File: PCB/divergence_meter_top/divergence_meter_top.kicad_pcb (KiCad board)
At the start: 2 copper layers, 120.6 x 38.1 mm, 11 parts

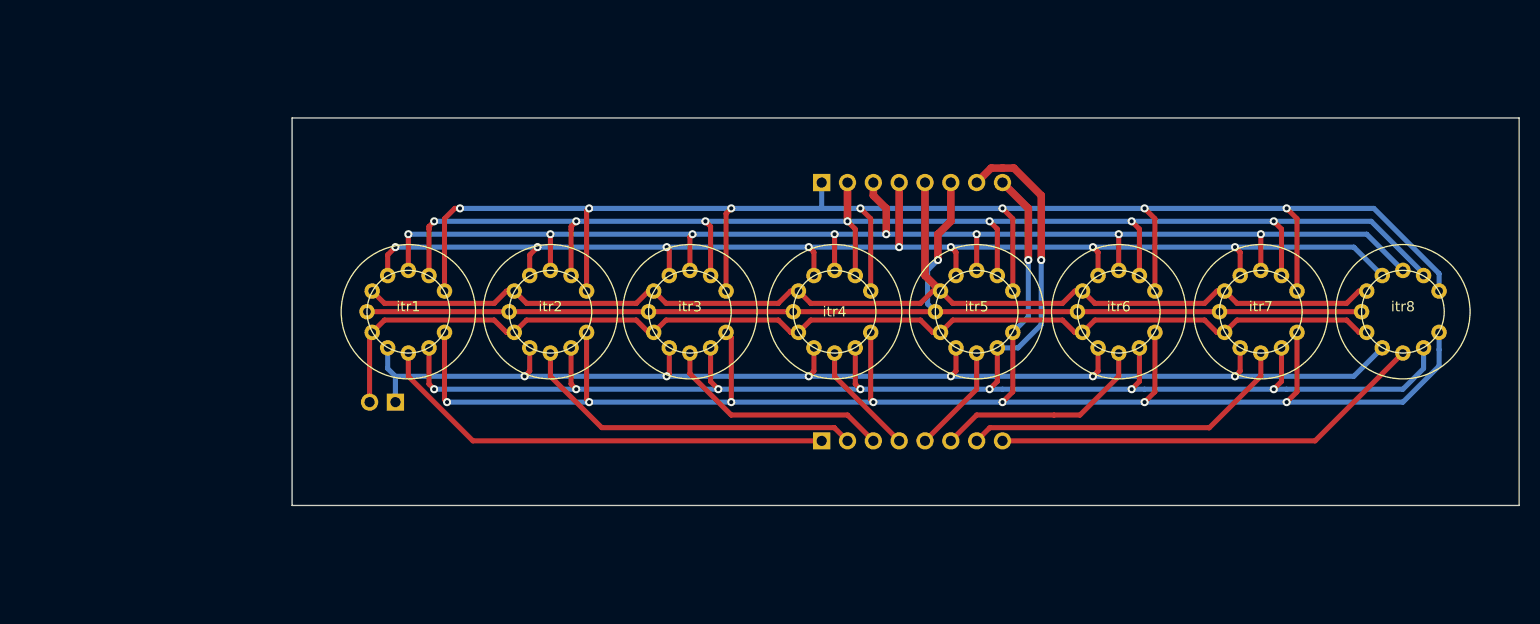
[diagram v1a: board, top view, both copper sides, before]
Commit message: logic pcb almost finished, remaking top
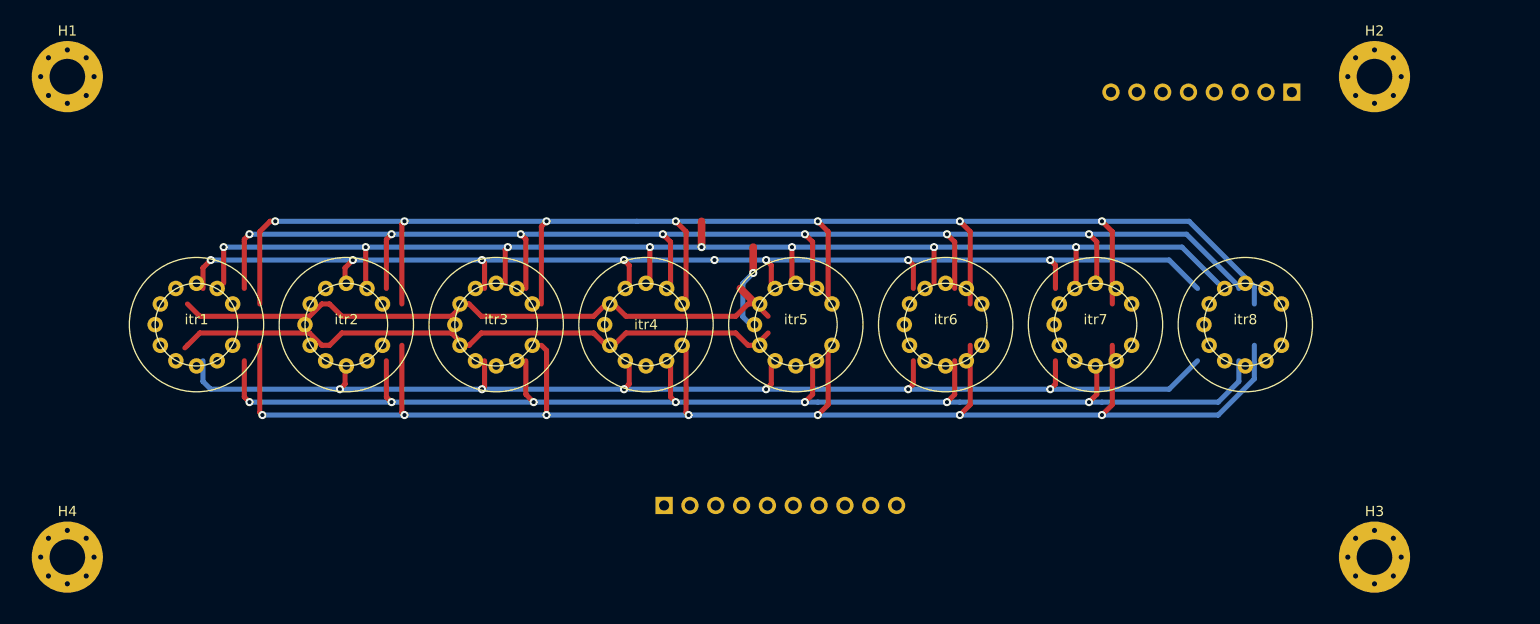
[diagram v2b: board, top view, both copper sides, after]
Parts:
- removed JG1: Conn_01x08, Connector_PinHeader_2.54mm:PinHeader_1x08_P2.54mm_Vertical
- removed JP1: 1V, Connector_PinHeader_2.54mm:PinHeader_1x02_P2.54mm_Vertical
- added H1: MountingHole_Pad, MountingHole:MountingHole_3.5mm_Pad_Via, F.Cu at (68.1, 84.8)
- added H2: MountingHole_Pad, MountingHole:MountingHole_3.5mm_Pad_Via, F.Cu at (196.6, 84.8)
- added H3: MountingHole_Pad, MountingHole:MountingHole_3.5mm_Pad_Via, F.Cu at (196.6, 132.1)
- added H4: MountingHole_Pad, MountingHole:MountingHole_3.5mm_Pad_Via, F.Cu at (68.1, 132.1)
- added JT1: Conn_01x10, Connector_PinHeader_2.54mm:PinHeader_1x10_P2.54mm_Vertical, B.Cu at (126.7, 127.0)
- moved JT2 47.1 mm to (188.5, 86.4), turned to 90 degrees
- moved itr1 20.9 mm to (80.8, 109.2)
- moved itr2 20.1 mm to (95.5, 109.2)
- moved itr3 19.1 mm to (110.2, 109.2)
- moved itr4 18.6 mm to (125.0, 109.2)
- moved itr5 17.8 mm to (139.7, 109.2)
- moved itr6 17.1 mm to (154.4, 109.2)
- moved itr7 16.3 mm to (169.2, 109.2)
- moved itr8 15.5 mm to (183.9, 109.2)
- renumbered JS1 to JT2
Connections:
- net Net-(JP1-Pad1) renamed +1V5
- net Net-(JP1-Pad2) renamed GND1
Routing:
- net Net-(JT2-Pad6): track 111.8 -> 8.36 mm
- net Net-(JT2-Pad5): track 116.1 -> 63.8 mm
- net GND1: track 111.8 -> 62.0 mm
- net Net-(itr1-Pad9): track 45.6 -> 0.00 mm
- net Net-(itr8-Pad9): track 42.9 -> 0.00 mm
- net Net-(itr2-Pad9): track 34.1 -> 0.00 mm
- net Net-(itr7-Pad9): track 32.8 -> 0.00 mm
- net Net-(JT2-Pad7): track 156.5 -> 130.5 mm, vias 8 -> 7
- net Net-(itr3-Pad9): track 22.8 -> 0.00 mm
- net Net-(itr6-Pad9): track 21.4 -> 0.00 mm
- net Net-(JT2-Pad8): track 168.5 -> 152.1 mm, vias 8 -> 7
- net Net-(itr4-Pad9): track 11.3 -> 0.00 mm
- net Net-(itr5-Pad9): track 10.7 -> 0.00 mm
- net Net-(JT2-Pad4): track 125.3 -> 119.0 mm
- net Net-(JT2-Pad2): track 142.6 -> 138.8 mm
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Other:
- board outline removed
- board text removed: "@Toohka"

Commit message: top done, logic almost
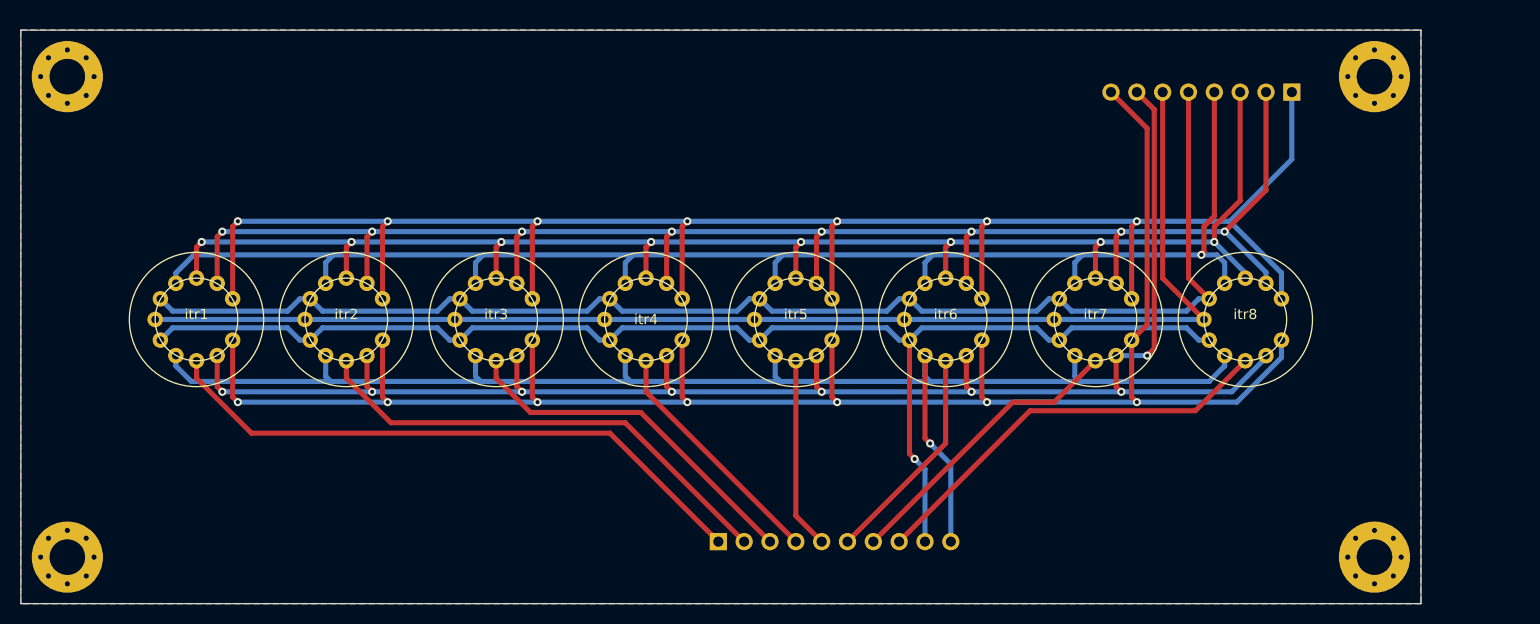
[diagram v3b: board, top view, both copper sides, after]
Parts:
- moved JT1 6.41 mm to (132.1, 130.6)
- moved itr1 0.51 mm to (80.8, 108.7)
- moved itr2 0.51 mm to (95.5, 108.7)
- moved itr3 0.51 mm to (110.2, 108.7)
- moved itr4 0.51 mm to (125.0, 108.7)
- moved itr5 0.51 mm to (139.7, 108.7)
- moved itr6 0.51 mm to (154.4, 108.7)
- moved itr7 0.51 mm to (169.2, 108.7)
- moved itr8 0.51 mm to (183.9, 108.7)
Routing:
- net Net-(JT2-Pad6): track 8.36 -> 127.2 mm, vias 1 -> 0
- net GND1: track 62.0 -> 131.4 mm, vias 0 -> 1
- net Net-(JT2-Pad5): track 63.8 -> 132.1 mm
- net Net-(itr1-Pad9): track 0.00 -> 59.7 mm
- net Net-(itr2-Pad9): track 0.00 -> 47.5 mm
- net Net-(itr8-Pad9): track 0.00 -> 41.4 mm
- net Net-(itr3-Pad9): track 0.00 -> 35.3 mm
- net Net-(JT2-Pad7): track 130.5 -> 160.5 mm, vias 7 -> 8
- net Net-(itr7-Pad9): track 0.00 -> 29.2 mm
- net Net-(JT2-Pad8): track 152.1 -> 176.8 mm
- net Net-(itr4-Pad9): track 0.00 -> 23.9 mm
- net Net-(JT2-Pad4): track 119.0 -> 142.4 mm, vias 8 -> 1
- net +1V5: track 119.2 -> 142.3 mm, vias 6 -> 1
- net Net-(itr6-Pad9): track 0.00 -> 21.8 mm
- net Net-(JT2-Pad3): track 126.8 -> 146.5 mm
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- added copper zone on B.Cu, net GND
- added copper zone on F.Cu, net GND
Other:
- board outline added: 137.7 x 56.4 mm

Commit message: PCB done, exported gerber
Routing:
- net Net-(JT2-Pad5): track 132.1 -> 131.3 mm
- net GND1: track 131.4 -> 130.6 mm
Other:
- board text added: "Toohka"
